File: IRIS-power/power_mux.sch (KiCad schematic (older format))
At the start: 12 parts, among them U31 TPS2121

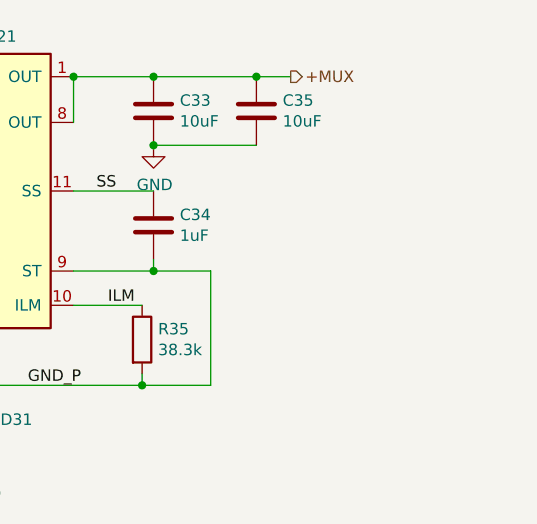
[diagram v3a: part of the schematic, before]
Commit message: Adjusted silkscreen
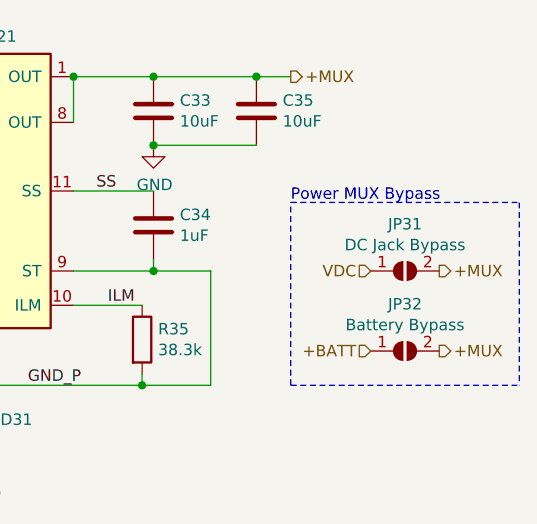
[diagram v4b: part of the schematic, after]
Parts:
- added JP31: DC Jack Bypass, Jumper:SolderJumper-2_P1.3mm_Open_RoundedPad1.0x1.5mm, symbol Jumper:SolderJumper_2_Open
- added JP32: Battery Bypass, Jumper:SolderJumper-2_P1.3mm_Open_RoundedPad1.0x1.5mm, symbol Jumper:SolderJumper_2_Open
- D31: footprint Diode_SMD:D_SMA_Handsoldering -> Diode_SMD:D_SMA
- R31, R34: Digikey PN (none) -> RNCP0603FTD2K49CT-ND
- R35: Digikey PN (none) -> RMCF0603FT38K3CT-ND
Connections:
- net +BATT: now also JP32.1 (A)
- net +MUX: now also JP31.2 (B), JP32.2 (B)
- net VDC: now also JP31.1 (A)
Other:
- note added: "Power MUX Bypass"
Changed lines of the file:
@@
 F 2 "Resistor_SMD:R_0603_1608Metric" V 5580 4250 50  0001 C CNN
 F 3 "~" H 5650 4250 50  0001 C CNN
+F 4 "RNCP0603FTD2K49CT-ND" H 5650 4250 50  0001 C CNN "Digikey PN"
 	1    5650 4250
 	1    0    0    -1
@@
 F 2 "Resistor_SMD:R_0603_1608Metric" V 7030 4450 50  0001 C CNN
 F 3 "~" H 7100 4450 50  0001 C CNN
+F 4 "RMCF0603FT38K3CT-ND" H 7100 4450 50  0001 C CNN "Digikey PN"
 	1    7100 4450
 	1    0    0    -1
@@
 F 2 "Resistor_SMD:R_0603_1608Metric" V 4680 3450 50  0001 C CNN
 F 3 "~" H 4750 3450 50  0001 C CNN
+F 4 "RNCP0603FTD2K49CT-ND" H 4750 3450 50  0001 C CNN "Digikey PN"
 	1    4750 3450
 	1    0    0    -1
@@
 F 0 "D31" V 6400 4650 50  0000 C CNN
 F 1 "D_Schottky" H 6400 4674 50  0001 C CNN
-F 2 "Diode_SMD:D_SMA_Handsoldering" H 6400 4800 50  0001 C CNN
+F 2 "Diode_SMD:D_SMA" H 6400 4800 50  0001 C CNN
 F 3 "https://www.comchiptech.com/admin/files/product/CDBA240LL-HF%20RevD765674.pdf" H 6400 4800 50  0001 C CNN
 F 4 "641-1698-1-ND" H 6400 4800 50  0001 C CNN "Digikey PN"
@@
 	7600 3600 7150 3600
 Connection ~ 7150 3600
+$Comp
+L Jumper:SolderJumper_2_Open JP31
+U 1 1 5FAA1238
+P 8250 4150
+F 0 "JP31" H 8250 4355 50  0000 C CNN
+F 1 "DC Jack Bypass" H 8250 4264 50  0000 C CNN
+F 2 "Jumper:SolderJumper-2_P1.3mm_Open_RoundedPad1.0x1.5mm" H 8250 4150 50  0001 C CNN
+F 3 "~" H 8250 4150 50  0001 C CNN
+	1    8250 4150
+	1    0    0    -1
+$EndComp
+Text HLabel 8400 4150 2    50   Output ~ 0
++MUX
+Text HLabel 8100 4150 0    50   Input ~ 0
+VDC
+$Comp
+L Jumper:SolderJumper_2_Open JP32
+U 1 1 5FAA1C70
+P 8250 4500
+F 0 "JP32" H 8250 4705 50  0000 C CNN
+F 1 "Battery Bypass" H 8250 4614 50  0000 C CNN
+F 2 "Jumper:SolderJumper-2_P1.3mm_Open_RoundedPad1.0x1.5mm" H 8250 4500 50  0001 C CNN
+F 3 "~" H 8250 4500 50  0001 C CNN
+	1    8250 4500
+	1    0    0    -1
+$EndComp
+Text HLabel 8400 4500 2    50   Output ~ 0
++MUX
+Text HLabel 8100 4500 0    50   Input ~ 0
++BATT
+Text Notes 7750 3850 0    50   ~ 0
+Power MUX Bypass
+Wire Notes Line
+	8750 3850 8750 4650
+Wire Notes Line
+	7750 4650 7750 3850
+Wire Notes Line
+	7750 3850 8750 3850
+Wire Notes Line
+	7750 4650 8750 4650
 $EndSCHEMATC

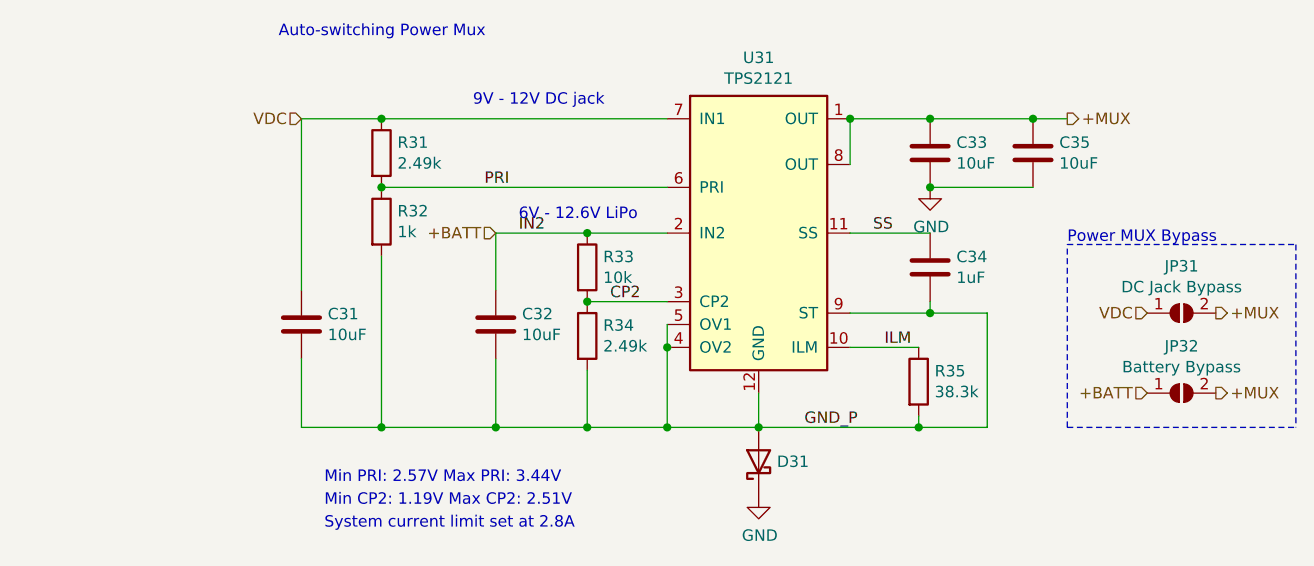
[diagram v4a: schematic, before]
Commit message: USB C power prototype
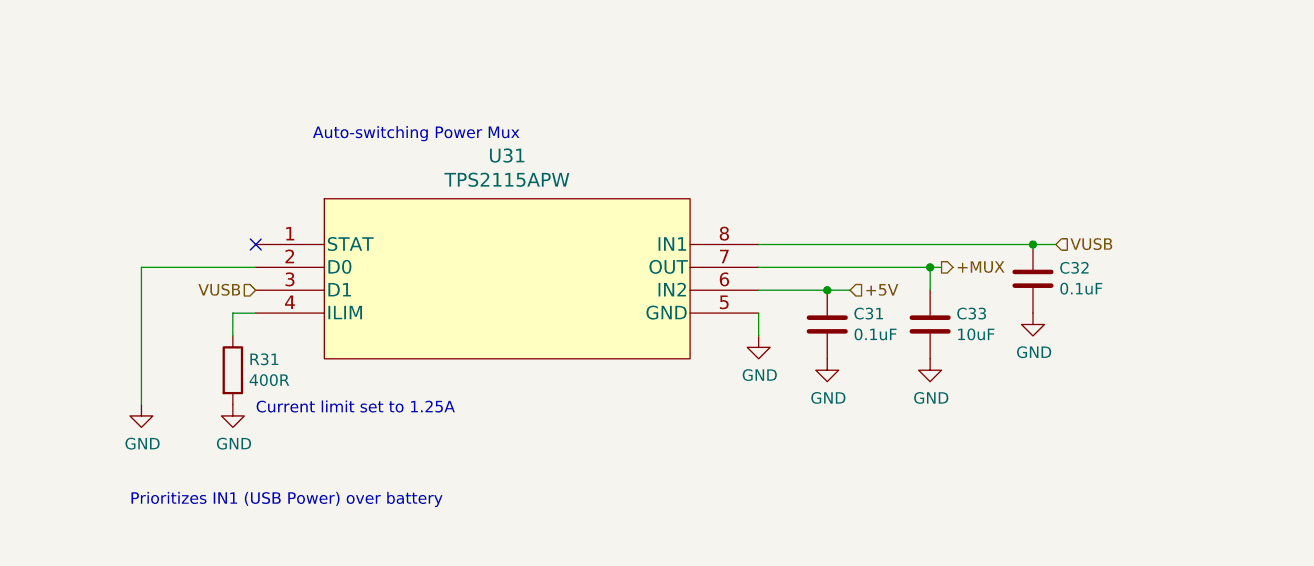
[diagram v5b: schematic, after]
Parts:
- removed C34: 1uF, Capacitor_SMD:C_0603_1608Metric, symbol Device:C
- removed C35: 10uF, Capacitor_SMD:C_0603_1608Metric, symbol Device:C
- removed D31: D_Schottky, Diode_SMD:D_SMA, symbol Device:D_Schottky
- removed JP31: DC Jack Bypass, Jumper:SolderJumper-2_P1.3mm_Open_RoundedPad1.0x1.5mm, symbol Jumper:SolderJumper_2_Open
- removed JP32: Battery Bypass, Jumper:SolderJumper-2_P1.3mm_Open_RoundedPad1.0x1.5mm, symbol Jumper:SolderJumper_2_Open
- removed R32: 1k, Resistor_SMD:R_0603_1608Metric, symbol Device:R
- removed R33: 10k, Resistor_SMD:R_0603_1608Metric, symbol Device:R
- removed R34: 2.49k, Resistor_SMD:R_0603_1608Metric, symbol Device:R
- removed R35: 38.3k, Resistor_SMD:R_0603_1608Metric, symbol Device:R
- removed U31: TPS2121, star-common-lib:TPS2121, symbol star-common-lib:TPS2121
- added U31: TPS2115APW, Package_SO:TSSOP-8_4.4x3mm_P0.65mm, symbol star-common-lib:TPS2115APW
- C31, C32: value 10uF -> 0.1uF; Digikey PN 1276-1192-1-ND -> (none)
- C33: Digikey PN 1276-1192-1-ND -> (none)
- R31: value 2.49k -> 400R; Digikey PN RNCP0603FTD2K49CT-ND -> (none)
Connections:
- net GND_P is gone; now on net GND: C31.2, C32.2
- net PRI is gone; now on net GND: R31.2
- net +MUX: now also U31.7 (OUT)
- net GND: now also U31.2 (D0), U31.5 (GND)
- net +BATT renamed VUSB
- net VUSB: now also U31.3 (D1), U31.8 (IN1)
- net VDC: no longer names the net of R31.1
- net VDC: now also U31.4 (ILIM); no longer C31.1
- new net +5V: C31.1, U31.6 (IN2)
- no-connect marks 0 -> 1
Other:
- note added: "Current limit set to 1.25A"
- note added: "Prioritizes IN1 (USB Power) over battery"
- note removed: "6V - 12.6V LiPo"
- note removed: "9V - 12V DC jack"
- note removed: "Min CP2: 1.19V Max CP2: 2.51V"
- note removed: "Min PRI: 2.57V Max PRI: 3.44V"
- note removed: "Power MUX Bypass"
- note removed: "System current limit set at 2.8A"

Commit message: Updated to V4.01
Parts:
- C31, C32: Digikey PN (none) -> 1276-CL10B104KB8NNNLCT-ND
- C33: Digikey PN (none) -> 1276-1192-1-ND
- R31: value 400R -> 402R; Digikey PN (none) -> RR08P402DCT-ND
- U31: Digikey PN (none) -> 296-16940-1-ND
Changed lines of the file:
@@
 F 2 "Package_SO:TSSOP-8_4.4x3mm_P0.65mm" H 5300 4090 60  0001 C CNN
 F 3 "" H 4200 3850 60  0000 C CNN
+F 4 "296-16940-1-ND" H 4200 3850 50  0001 C CNN "Digikey PN"
 	1    4200 3850
 	1    0    0    -1
@@
 F 2 "Capacitor_SMD:C_0603_1608Metric" H 7638 3850 50  0001 C CNN
 F 3 "~" H 7600 4000 50  0001 C CNN
+F 4 "1276-CL10B104KB8NNNLCT-ND" H 7600 4000 50  0001 C CNN "Digikey PN"
 	1    7600 4000
 	1    0    0    -1
@@
 F 2 "Capacitor_SMD:C_0603_1608Metric" H 6738 4050 50  0001 C CNN
 F 3 "~" H 6700 4200 50  0001 C CNN
+F 4 "1276-CL10B104KB8NNNLCT-ND" H 6700 4200 50  0001 C CNN "Digikey PN"
 	1    6700 4200
 	1    0    0    -1
@@
 P 4100 4400
 F 0 "R31" H 4170 4446 50  0000 L CNN
-F 1 "400R" H 4170 4355 50  0000 L CNN
+F 1 "402R" H 4170 4355 50  0000 L CNN
 F 2 "Resistor_SMD:R_0603_1608Metric" V 4030 4400 50  0001 C CNN
 F 3 "~" H 4100 4400 50  0001 C CNN
+F 4 "RR08P402DCT-ND" H 4100 4400 50  0001 C CNN "Digikey PN"
 	1    4100 4400
 	1    0    0    -1
@@
 F 2 "Capacitor_SMD:C_0603_1608Metric" H 7188 4050 50  0001 C CNN
 F 3 "~" H 7150 4200 50  0001 C CNN
+F 4 "1276-1192-1-ND" H 7150 4200 50  0001 C CNN "Digikey PN"
 	1    7150 4200
 	1    0    0    -1

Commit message: IRIS V4.02
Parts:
- added R32: 10k, Resistor_SMD:R_0603_1608Metric, symbol Device:R
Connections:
- net GND: now also R32.2
- net VUSB: now also R32.1
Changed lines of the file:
@@
 Text Notes 4200 4600 0    50   ~ 0
 Current limit set to 1.25A
-Wire Wire Line
-	4200 3950 3700 3950
 $Comp
 L power:GND #PWR031
 U 1 1 5FBB6394
-P 3700 4550
-F 0 "#PWR031" H 3700 4300 50  0001 C CNN
-F 1 "GND" H 3705 4377 50  0000 C CNN
-F 2 "" H 3700 4550 50  0001 C CNN
-F 3 "" H 3700 4550 50  0001 C CNN
-	1    3700 4550
+P 3250 4550
+F 0 "#PWR031" H 3250 4300 50  0001 C CNN
+F 1 "GND" H 3255 4377 50  0000 C CNN
+F 2 "" H 3250 4550 50  0001 C CNN
+F 3 "" H 3250 4550 50  0001 C CNN
+	1    3250 4550
 	1    0    0    -1
 $EndComp
 Wire Wire Line
-	3700 3950 3700 4550
-Text HLabel 4200 4050 0    50   Input ~ 0
+	3250 3950 3250 4550
+Text HLabel 3600 4050 0    50   Input ~ 0
 VUSB
 Text Notes 3650 5000 0    50   ~ 0
@@
 Wire Wire Line
 	6400 3850 7600 3850
+$Comp
+L Device:R R32
+U 1 1 5FEFD5D1
+P 3800 4400
+F 0 "R32" H 3870 4446 50  0000 L CNN
+F 1 "10k" H 3870 4355 50  0000 L CNN
+F 2 "Resistor_SMD:R_0603_1608Metric" V 3730 4400 50  0001 C CNN
+F 3 "~" H 3800 4400 50  0001 C CNN
+	1    3800 4400
+	1    0    0    -1
+$EndComp
+Wire Wire Line
+	3250 3950 4200 3950
+Wire Wire Line
+	3600 4050 3800 4050
+$Comp
+L power:GND #PWR0109
+U 1 1 5FEFEBA9
+P 3800 4550
+F 0 "#PWR0109" H 3800 4300 50  0001 C CNN
+F 1 "GND" H 3805 4377 50  0000 C CNN
+F 2 "" H 3800 4550 50  0001 C CNN
+F 3 "" H 3800 4550 50  0001 C CNN
+	1    3800 4550
+	1    0    0    -1
+$EndComp
+Wire Wire Line
+	3800 4250 3800 4050
+Connection ~ 3800 4050
+Wire Wire Line
+	3800 4050 4200 4050
 $EndSCHEMATC
